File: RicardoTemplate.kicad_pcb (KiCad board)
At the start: 4 copper layers, 40.6 x 62.6 mm, 134 parts, among them IC2 SX1280, J1 RBUS, J2 USB_C_Receptacle_USB2.0, U1 ESP32-S3, U11 SC4215ASTRT, U12 SKY66112-11, U13 DEA202450BT-1213C1, U2 SN65HVD230, U3 LM66200DRLR, U4 MAX77827AEFD+T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

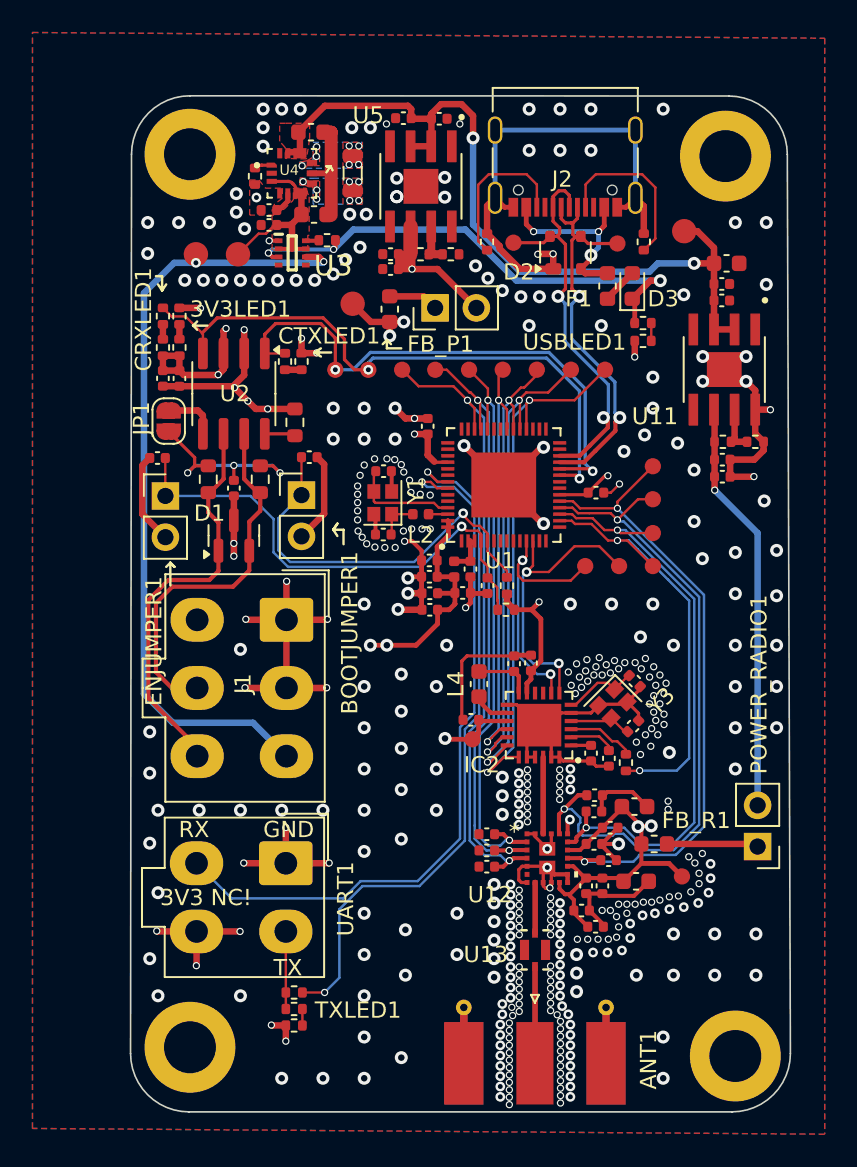
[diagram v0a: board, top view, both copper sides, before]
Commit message: Added Faraday cage around PCB edge
Less emi more betterer
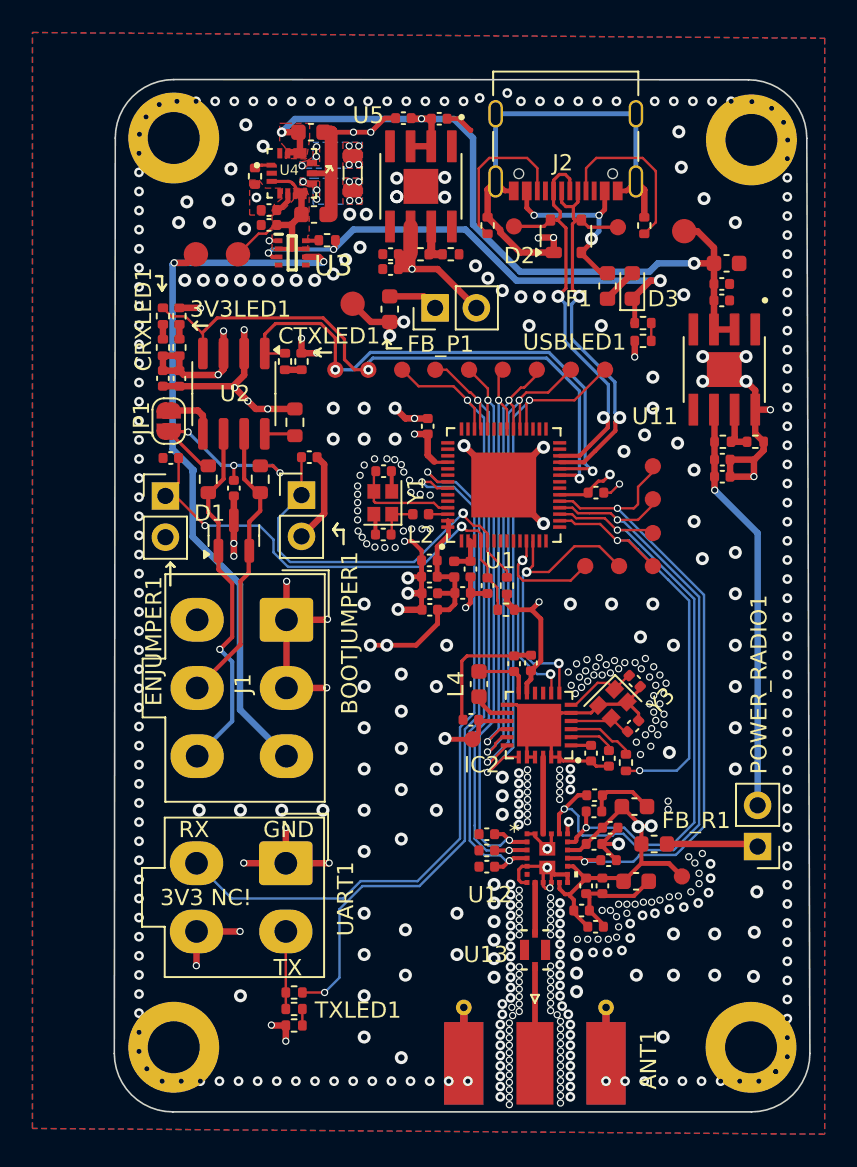
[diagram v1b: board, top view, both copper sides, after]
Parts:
- moved H2 1.89 mm to (157.7, 74.7)
- moved H1 1.41 mm to (122.1, 74.6)
- moved H4 1.10 mm to (157.7, 130.6)
- moved J2 1.01 mm to (146.3, 75.3)
- moved D+_TP1 1.01 mm to (143.1, 80.0)
- moved D2 1.01 mm to (146.3, 80.6)
- moved R11 1.01 mm to (151.1, 80.0)
- moved R12 1.01 mm to (141.5, 80.0)
- moved D-_TP1 1.01 mm to (149.5, 80.1)
- moved H3 1.00 mm to (122.1, 130.6)
- moved C3 0.82 mm to (121.9, 94.3)
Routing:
- net GND: track 211.5 -> 401.7 mm, vias 408 -> 538
- net /CAN+: track 23.0 -> 17.8 mm
- net RBUS_uC_V: track 48.7 -> 45.4 mm
- net /CAN-: track 25.1 -> 22.4 mm, vias 0 -> 1
- net +3V3: track 56.3 -> 53.8 mm, vias 16 -> 15
- net /Data+: track 24.9 -> 25.9 mm
- net /Data-: track 24.3 -> 25.3 mm
- net Net-(JP1-B): track 12.6 -> 13.5 mm
- net CPS: track 39.3 -> 39.9 mm
- net +VDC: track 49.4 -> 50.0 mm, vias 2 -> 3
- net /CHIP_PU: track 31.1 -> 30.7 mm, vias 1 -> 2
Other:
- board size 40.6 x 62.6 mm -> 42.8 x 63.6 mm

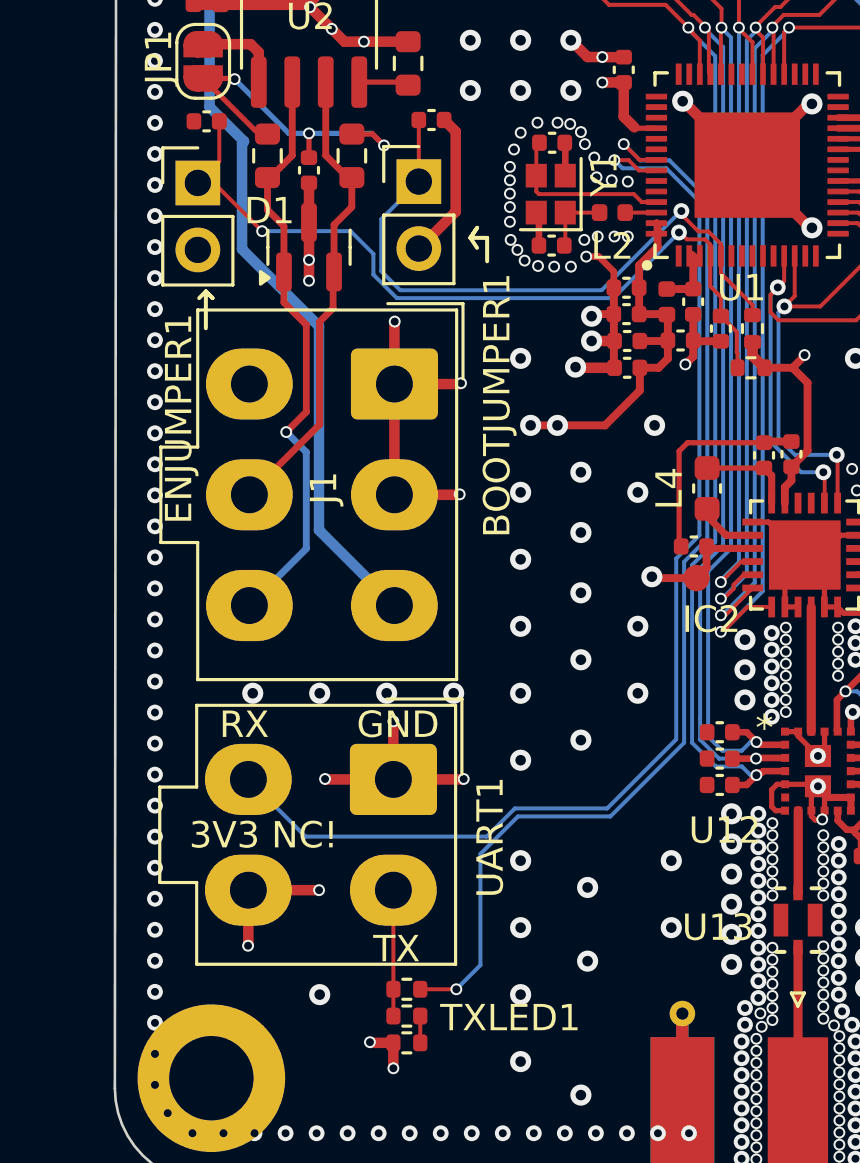
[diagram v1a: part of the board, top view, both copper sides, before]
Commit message: Changed UART connector
Now with 1000% more nanofit!
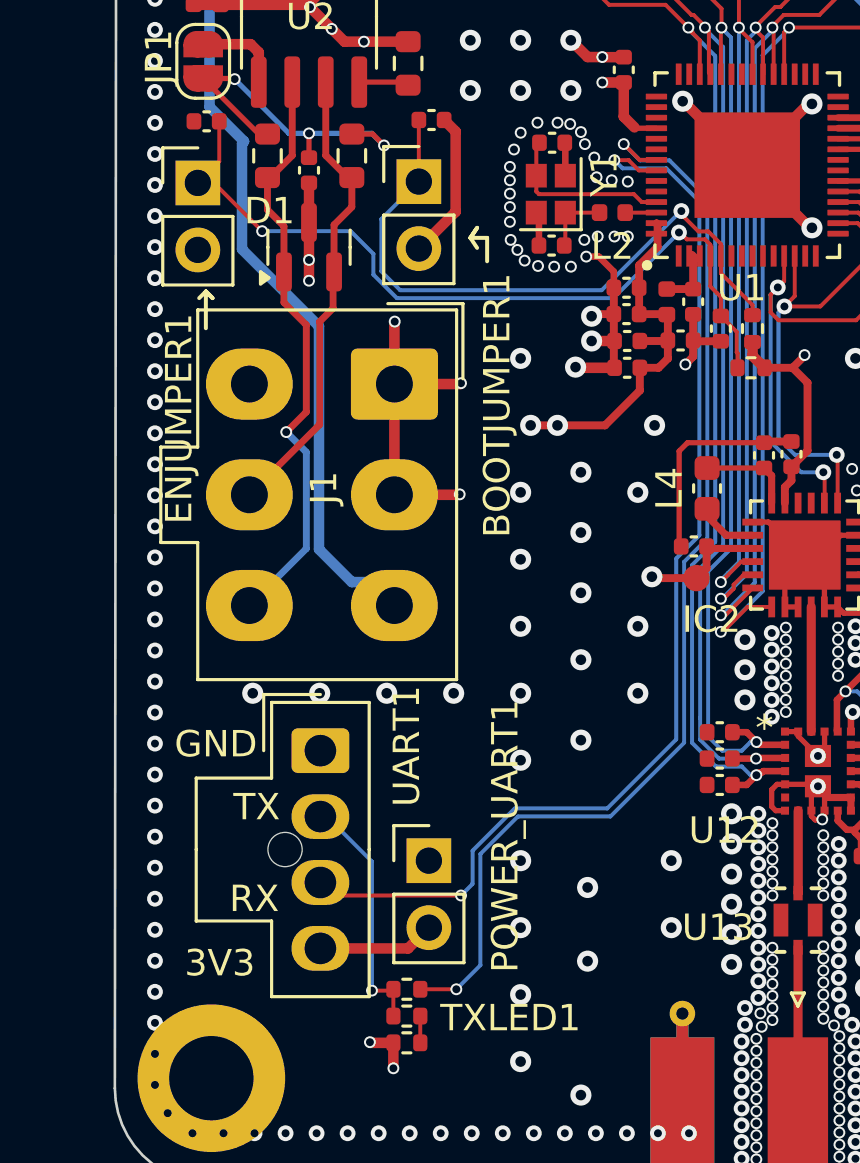
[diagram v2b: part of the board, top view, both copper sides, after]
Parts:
- added G***: LOGO, footprints:rae_logo_6mm, B.Cu at (134.9, 130.9)
- added POWER_UART1: Conn_01x02_Male, Connector_PinHeader_2.54mm:PinHeader_1x02_P2.54mm_Vertical, F.Cu at (130.4, 122.3)
- UART1: footprint Connector_Molex:Molex_Mini-Fit_Jr_5566-04A_2x02_P4.20mm_Vertical -> Connector_Molex:Molex_Nano-Fit_105309-xx04_1x04_P2.50mm_Vertical
- moved UART1 2.98 mm to (126.3, 118.2), turned to 0 degrees
- moved G*** 0.90 mm to (128.6, 130.8)
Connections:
- UART1 pad 4: +3V3 -> Net-(POWER_UART1-Pin_2)
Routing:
- net GND: track 401.7 -> 394.3 mm, vias 538 -> 534
- net +3V3: track 53.8 -> 49.0 mm, vias 15 -> 13
- net /TXD: track 4.78 -> 9.41 mm, vias 0 -> 1
- net Net-(POWER_UART1-Pin_2): track 0.00 -> 4.44 mm
- net /RXD: track 45.0 -> 43.3 mm, vias 1 -> 2
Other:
- board text added: "3V3"
- board text removed: "3V3 NC!"

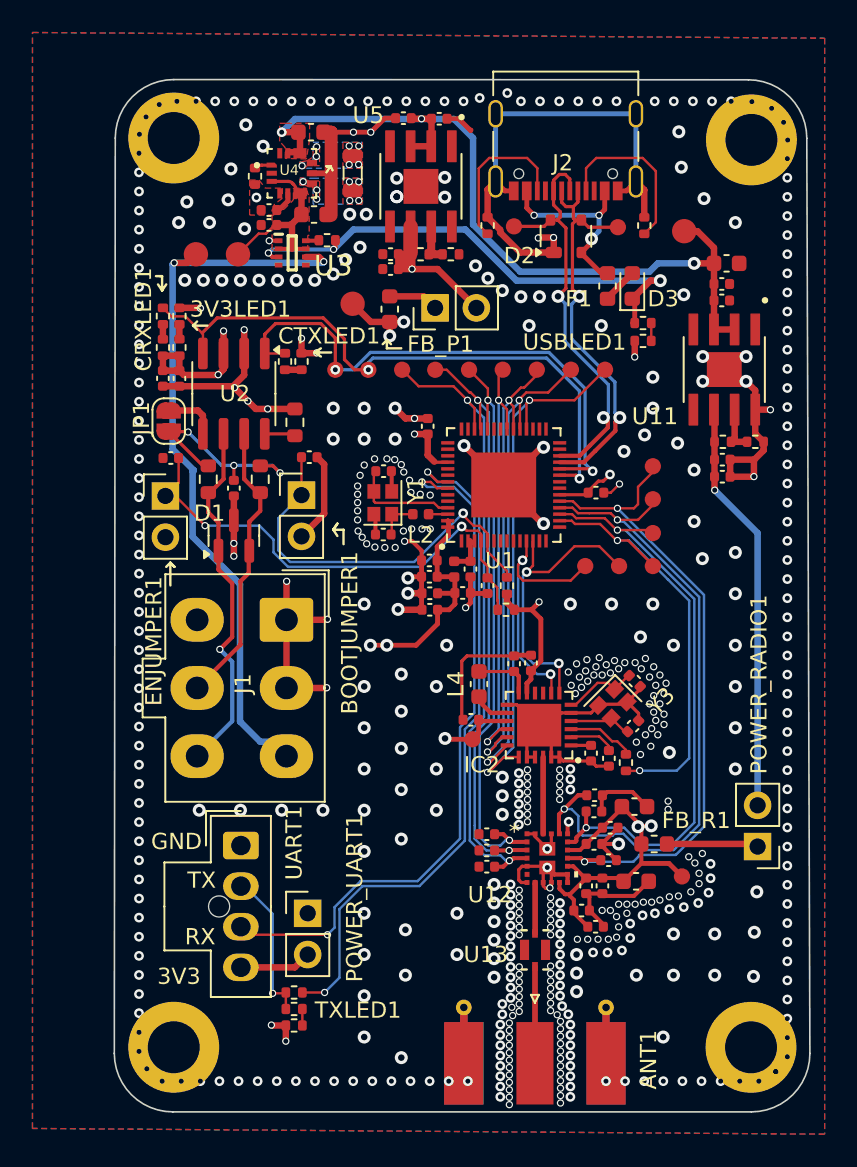
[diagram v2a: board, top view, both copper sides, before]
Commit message: Changed uart conn
Get transposed!
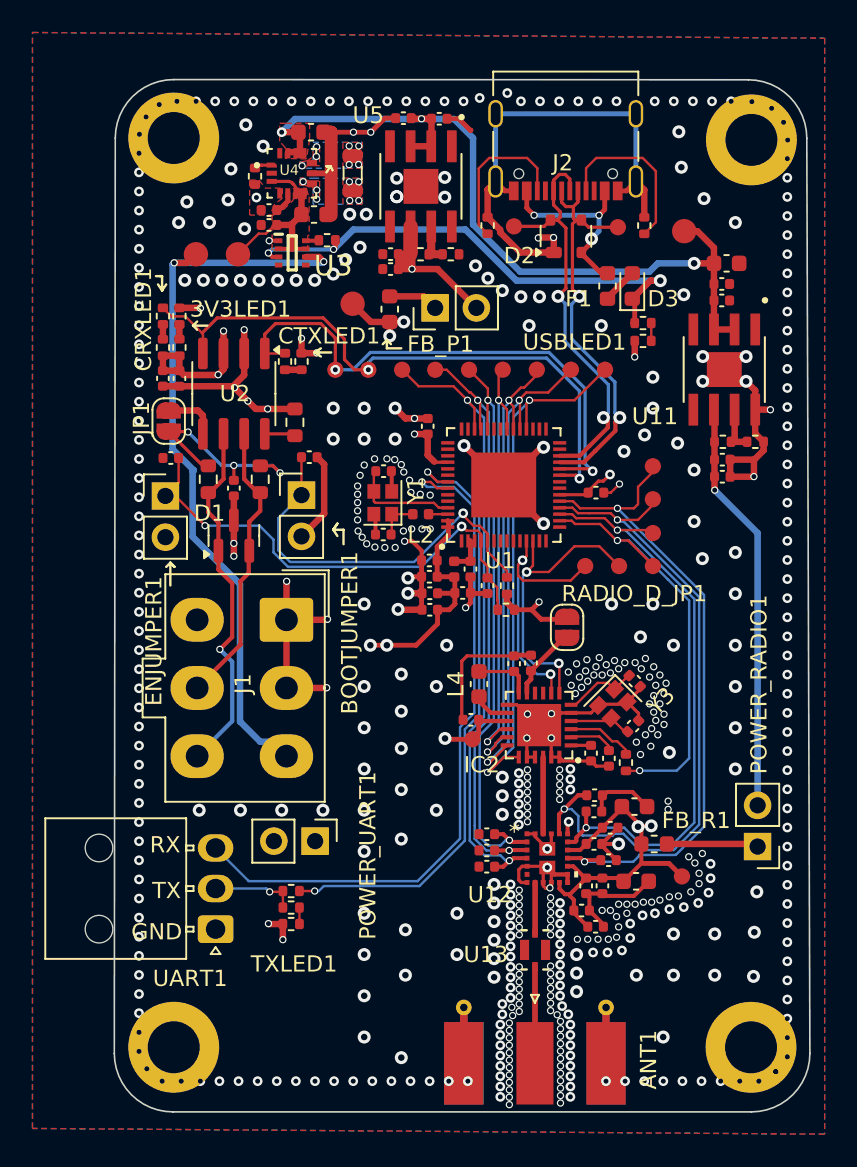
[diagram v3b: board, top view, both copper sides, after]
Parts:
- added RADIO_D_JP1: j, Jumper:SolderJumper-2_P1.3mm_Open_RoundedPad1.0x1.5mm, F.Cu at (146.4, 104.7)
- UART1: footprint Connector_Molex:Molex_Nano-Fit_105309-xx04_1x04_P2.50mm_Vertical -> Connector_Molex:Molex_Nano-Fit_105313-xx03_1x03_P2.50mm_Horizontal
- moved R6 6.25 mm to (129.4, 121.0)
- moved TXLED1 6.25 mm to (129.4, 122.0)
- moved R2 6.25 mm to (129.4, 123.0)
- moved UART1 5.38 mm to (124.7, 123.3), turned to 180 degrees
- moved POWER_UART1 4.47 mm to (130.8, 117.9), turned to -90 degrees
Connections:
- C54 pad 1: +3V3 -> Net-(IC2-VBAT_IO)
- IC2 pad 11: +3V3 -> Net-(IC2-VBAT_IO)
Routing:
- net Net-(U1-U0TXD/PROG/GPIO43): track 42.9 -> 38.0 mm
- net Net-(IC2-VBAT_IO): track 0.00 -> 4.54 mm
- net Net-(POWER_UART1-Pin_2): track 4.44 -> 0.00 mm
- net /TXD: track 9.41 -> 5.27 mm
- net +3V3: track 49.0 -> 45.8 mm
- net /RXD: track 43.3 -> 43.4 mm, vias 2 -> 1
- net GND: vias 534 -> 537
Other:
- board text removed: "3V3"
